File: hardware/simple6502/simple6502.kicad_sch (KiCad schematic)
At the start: 20 parts, among them J1 ~{VP}, J2 CLK SEL, J3 RESET, J7 FTDI Serial, J8 USB Power, SW1 RESET, T1 DS1813-10+, U1 W65C02SxP, U2 RAM 62256, U3 ROM 28C256, U4 74LS30, U5 74HCT00, U6 74HC138, U7 MC68B50, X1 ACO-1MHz

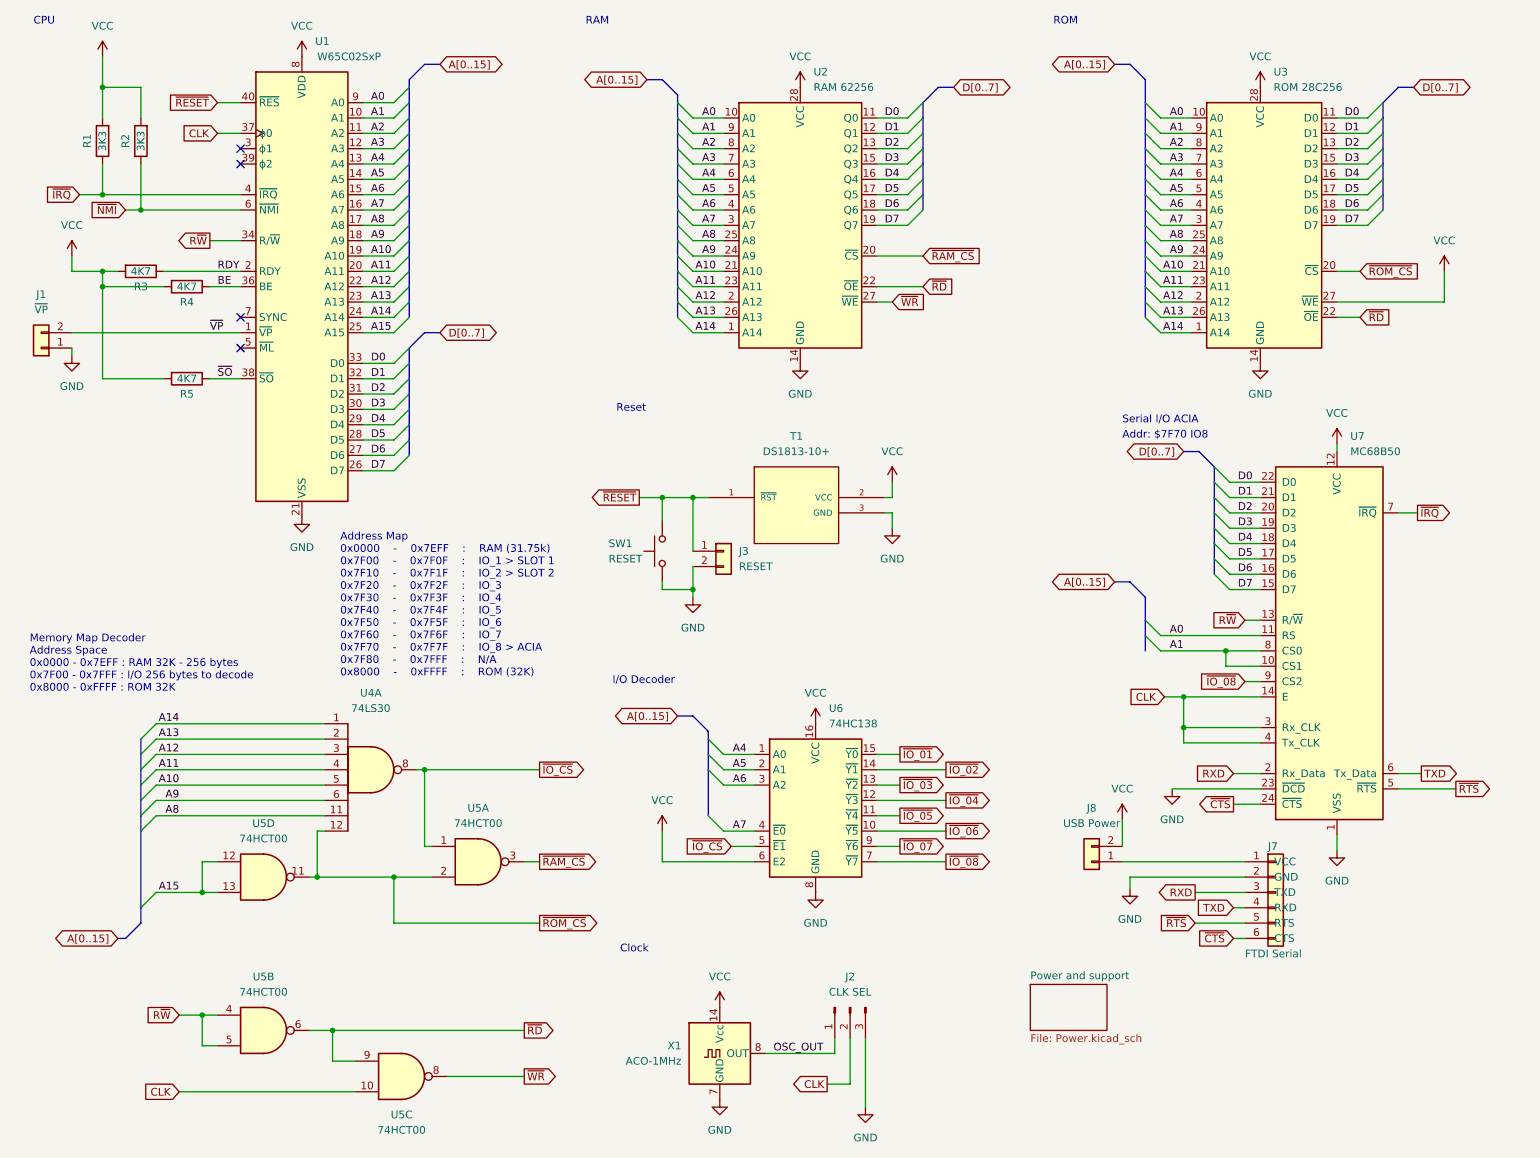
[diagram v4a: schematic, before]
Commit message: renumer components based on PCB placement
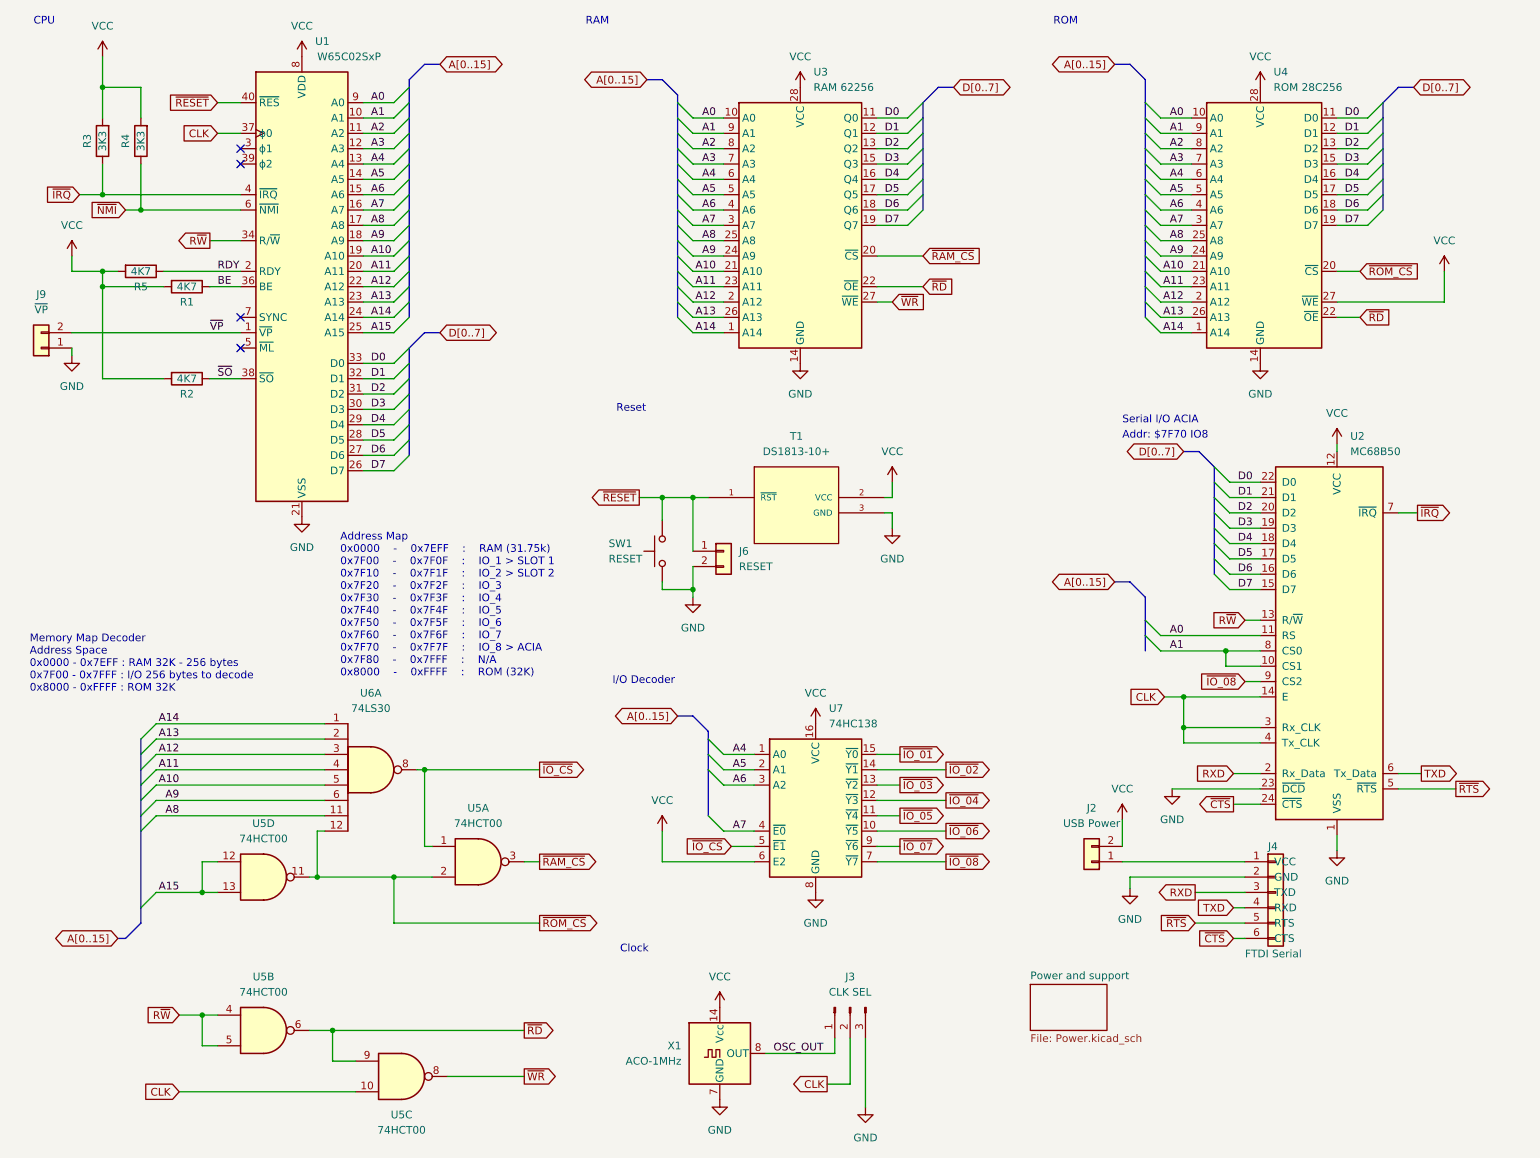
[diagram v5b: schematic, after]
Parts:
- renumbered J8 to J2, J2 to J3, J7 to J4, J3 to J6, J1 to J9, R4 to R1, R5 to R2, R1 to R3, R2 to R4, R3 to R5, U7 to U2, U2 to U3, U3 to U4, U4 to U6, U6 to U7
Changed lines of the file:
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@@
   (symbol (lib_id "Connector:Conn_01x03_Pin") (at 150.495 179.07 90) (mirror x) (unit 1)
     (in_bom yes) (on_board yes) (dnp no)
-    (property "Reference" "J2" (at 150.495 173.99 90)
+    (property "Reference" "J3" (at 150.495 173.99 90)
       (effects (font (size 1.27 1.27)))
     )
@@
       (project "simple6502"
         (path "/c0007eb4-077e-4f77-aad9-8dd15548af06"
-          (reference "J2") (unit 1)
+          (reference "J3") (unit 1)
         )
       )
@@
   (symbol (lib_name "R_1") (lib_id "Device:R") (at 40.64 59.69 270) (unit 1)
     (in_bom yes) (on_board yes) (dnp no)
-    (property "Reference" "R4" (at 40.64 62.23 90)
+    (property "Reference" "R1" (at 40.64 62.23 90)
       (effects (font (size 1.27 1.27)))
     )
@@
       (project "simple6502"
         (path "/c0007eb4-077e-4f77-aad9-8dd15548af06"
-          (reference "R4") (unit 1)
+          (reference "R1") (unit 1)
         )
       )
@@
   (symbol (lib_id "74xx:74LS30") (at 71.12 139.7 0) (unit 1)
     (in_bom yes) (on_board yes) (dnp no) (fields_autoplaced)
-    (property "Reference" "U4" (at 71.1117 127 0)
+    (property "Reference" "U6" (at 71.1117 127 0)
       (effects (font (size 1.27 1.27)))
     )
@@
       (project "simple6502"
         (path "/c0007eb4-077e-4f77-aad9-8dd15548af06"
-          (reference "U4") (unit 1)
+          (reference "U6") (unit 1)
         )
       )
@@
   (symbol (lib_name "R_1") (lib_id "Device:R") (at 26.67 35.56 180) (unit 1)
     (in_bom yes) (on_board yes) (dnp no)
-    (property "Reference" "R1" (at 24.13 35.56 90)
+    (property "Reference" "R3" (at 24.13 35.56 90)
       (effects (font (size 1.27 1.27)))
     )
@@
       (project "simple6502"
         (path "/c0007eb4-077e-4f77-aad9-8dd15548af06"
-          (reference "R1") (unit 1)
+          (reference "R3") (unit 1)
         )
       )
@@
   (symbol (lib_id "Memory_RAM:CY62256-70PC") (at 142.24 49.53 0) (unit 1)
     (in_bom yes) (on_board yes) (dnp no) (fields_autoplaced)
-    (property "Reference" "U2" (at 144.4341 24.13 0)
+    (property "Reference" "U3" (at 144.4341 24.13 0)
       (effects (font (size 1.27 1.27)) (justify left))
     )
@@
       (project "simple6502"
         (path "/c0007eb4-077e-4f77-aad9-8dd15548af06"
-          (reference "U2") (unit 1)
+          (reference "U3") (unit 1)
         )
       )
@@
   (symbol (lib_id "Memory_EEPROM:28C256") (at 218.44 54.61 0) (unit 1)
     (in_bom yes) (on_board yes) (dnp no) (fields_autoplaced)
-    (property "Reference" "U3" (at 220.6341 24.13 0)
+    (property "Reference" "U4" (at 220.6341 24.13 0)
       (effects (font (size 1.27 1.27)) (justify left))
     )
@@
       (project "simple6502"
         (path "/c0007eb4-077e-4f77-aad9-8dd15548af06"
-          (reference "U3") (unit 1)
+          (reference "U4") (unit 1)
         )
       )
@@
   (symbol (lib_id "74xx:74HC138") (at 144.78 147.32 0) (unit 1)
     (in_bom yes) (on_board yes) (dnp no) (fields_autoplaced)
-    (property "Reference" "U6" (at 146.9741 129.54 0)
+    (property "Reference" "U7" (at 146.9741 129.54 0)
       (effects (font (size 1.27 1.27)) (justify left))
     )
@@
       (project "simple6502"
         (path "/c0007eb4-077e-4f77-aad9-8dd15548af06"
-          (reference "U6") (unit 1)
+          (reference "U7") (unit 1)
         )
       )
@@
   (symbol (lib_id "Connector_Generic:Conn_01x06") (at 220.98 160.02 0) (unit 1)
     (in_bom yes) (on_board yes) (dnp no) (fields_autoplaced)
-    (property "Reference" "J7" (at 219.71 152.4 0)
+    (property "Reference" "J4" (at 219.71 152.4 0)
       (effects (font (size 1.27 1.27)) (justify left))
     )
@@
       (project "simple6502"
         (path "/c0007eb4-077e-4f77-aad9-8dd15548af06"
-          (reference "J7") (unit 1)
+          (reference "J4") (unit 1)
         )
       )
@@
   (symbol (lib_name "R_1") (lib_id "Device:R") (at 33.02 57.15 270) (unit 1)
     (in_bom yes) (on_board yes) (dnp no)
-    (property "Reference" "R3" (at 33.02 59.69 90)
+    (property "Reference" "R5" (at 33.02 59.69 90)
       (effects (font (size 1.27 1.27)))
     )
@@
       (project "simple6502"
         (path "/c0007eb4-077e-4f77-aad9-8dd15548af06"
-          (reference "R3") (unit 1)
+          (reference "R5") (unit 1)
         )
       )
@@
   (symbol (lib_id "Connector_Generic:Conn_01x02") (at 190.5 154.94 180) (unit 1)
     (in_bom yes) (on_board yes) (dnp no) (fields_autoplaced)
-    (property "Reference" "J8" (at 190.5 146.05 0)
+    (property "Reference" "J2" (at 190.5 146.05 0)
       (effects (font (size 1.27 1.27)))
     )
@@
       (project "simple6502"
         (path "/c0007eb4-077e-4f77-aad9-8dd15548af06"
-          (reference "J8") (unit 1)
+          (reference "J2") (unit 1)
         )
       )
@@
   (symbol (lib_id "Connector_Generic:Conn_01x02") (at 129.54 103.505 0) (unit 1)
     (in_bom yes) (on_board yes) (dnp no) (fields_autoplaced)
-    (property "Reference" "J3" (at 132.08 103.505 0)
+    (property "Reference" "J6" (at 132.08 103.505 0)
       (effects (font (size 1.27 1.27)) (justify left))
     )
@@
       (project "simple6502"
         (path "/c0007eb4-077e-4f77-aad9-8dd15548af06"
-          (reference "J3") (unit 1)
+          (reference "J6") (unit 1)
         )
       )
@@
   (symbol (lib_id "Interface_UART:MC68B50") (at 231.14 120.015 0) (unit 1)
     (in_bom yes) (on_board yes) (dnp no) (fields_autoplaced)
-    (property "Reference" "U7" (at 233.3341 84.455 0)
+    (property "Reference" "U2" (at 233.3341 84.455 0)
       (effects (font (size 1.27 1.27)) (justify left))
     )
@@
       (project "simple6502"
         (path "/c0007eb4-077e-4f77-aad9-8dd15548af06"
-          (reference "U7") (unit 1)
+          (reference "U2") (unit 1)
         )
       )
@@
   (symbol (lib_id "Connector_Generic:Conn_01x02") (at 16.51 69.85 180) (unit 1)
     (in_bom yes) (on_board yes) (dnp no) (fields_autoplaced)
-    (property "Reference" "J1" (at 16.51 60.96 0)
+    (property "Reference" "J9" (at 16.51 60.96 0)
       (effects (font (size 1.27 1.27)))
     )
@@
       (project "simple6502"
         (path "/c0007eb4-077e-4f77-aad9-8dd15548af06"
-          (reference "J1") (unit 1)
+          (reference "J9") (unit 1)
         )
       )
@@
   (symbol (lib_name "R_1") (lib_id "Device:R") (at 33.02 35.56 180) (unit 1)
     (in_bom yes) (on_board yes) (dnp no)
-    (property "Reference" "R2" (at 30.48 35.56 90)
+    (property "Reference" "R4" (at 30.48 35.56 90)
       (effects (font (size 1.27 1.27)))
     )
@@
       (project "simple6502"
         (path "/c0007eb4-077e-4f77-aad9-8dd15548af06"
-          (reference "R2") (unit 1)
+          (reference "R4") (unit 1)
         )
       )
@@
   (symbol (lib_name "R_1") (lib_id "Device:R") (at 40.64 74.93 270) (unit 1)
     (in_bom yes) (on_board yes) (dnp no)
-    (property "Reference" "R5" (at 40.64 77.47 90)
+    (property "Reference" "R2" (at 40.64 77.47 90)
       (effects (font (size 1.27 1.27)))
     )
@@
       (project "simple6502"
         (path "/c0007eb4-077e-4f77-aad9-8dd15548af06"
-          (reference "R5") (unit 1)
-        )
-      )
+          (reference "R2") (unit 1)
+        )
+      )

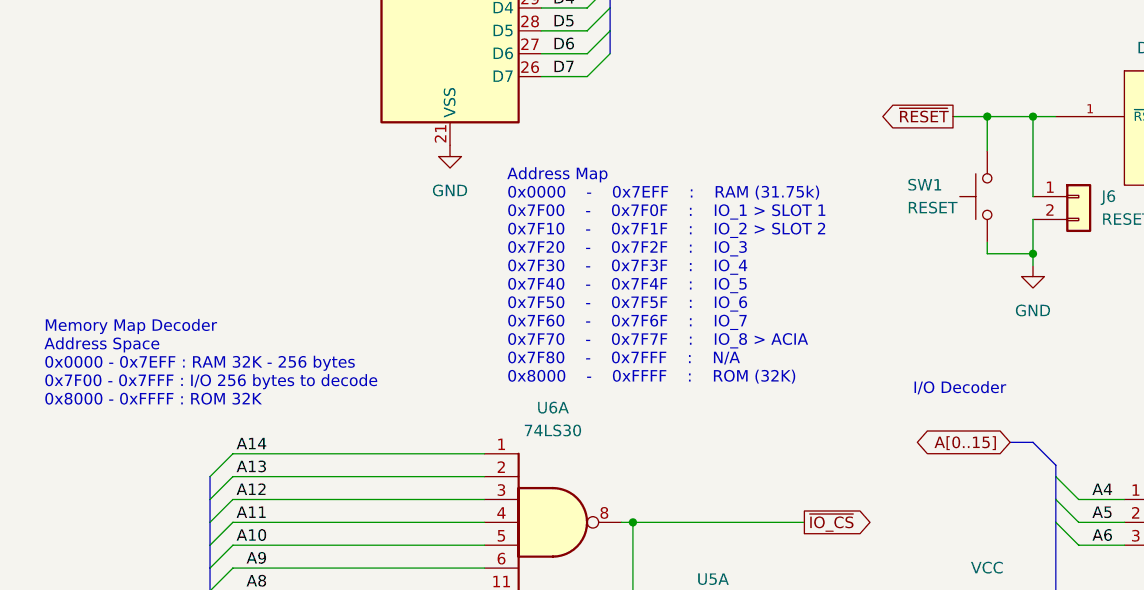
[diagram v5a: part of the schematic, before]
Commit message: updated ReadME and memory map in the schematic
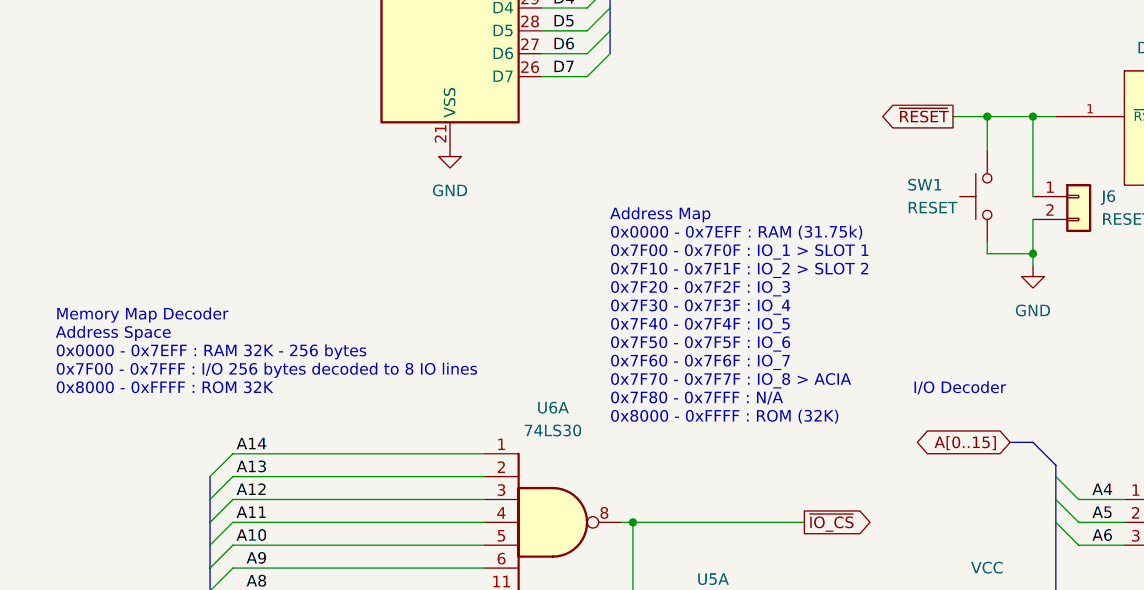
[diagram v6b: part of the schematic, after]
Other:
- note added: "Memory Map Decoder Address Space 0x0000 - 0x7EFF : RAM 32K - 256 bytes 0x7F00 - 0x7FFF : I/O 256 bytes decoded to 8 IO lines 0x8000 - 0xFFFF : ROM 32K"
- note removed: "Memory Map Decoder Address Space 0x0000 - 0x7EFF : RAM 32K - 256 bytes 0x7F00 - 0x7FFF : I/O 256 bytes to decode 0x8000 - 0xFFFF : ROM 32K"
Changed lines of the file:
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@@
     (effects (font (size 1.27 1.27)) (justify left bottom))
   )
-  (text "Memory Map Decoder\nAddress Space\n0x0000 - 0x7EFF : RAM 32K - 256 bytes\n0x7F00 - 0x7FFF : I/O 256 bytes to decode\n0x8000 - 0xFFFF : ROM 32K\n"
-    (at 14.605 127 0)
+  (text "Memory Map Decoder\nAddress Space\n0x0000 - 0x7EFF : RAM 32K - 256 bytes\n0x7F00 - 0x7FFF : I/O 256 bytes decoded to 8 IO lines\n0x8000 - 0xFFFF : ROM 32K\n"
+    (at 15.875 125.73 0)
     (effects (font (size 1.27 1.27)) (justify left bottom))
   )
@@
     (effects (font (size 1.27 1.27)) (justify left bottom))
   )
-  (text "Address Map				\n0x0000	-	0x7EFF	:	RAM (31.75k)\n0x7F00	-	0x7F0F	:	IO_1 > SLOT 1\n0x7F10	-	0x7F1F	:	IO_2 > SLOT 2\n0x7F20	-	0x7F2F	:	IO_3\n0x7F30	-	0x7F3F	:	IO_4\n0x7F40	-	0x7F4F	:	IO_5\n0x7F50	-	0x7F5F	:	IO_6\n0x7F60	-	0x7F6F	:	IO_7\n0x7F70	-	0x7F7F	:	IO_8 > ACIA\n0x7F80	-	0x7FFF	:	N/A\n0x8000	-	0xFFFF	:	ROM (32K)"
-    (at 66.04 124.46 0)
+  (text "Address Map				\n0x0000 - 0x7EFF : RAM (31.75k)\n0x7F00 - 0x7F0F : IO_1 > SLOT 1\n0x7F10 - 0x7F1F : IO_2 > SLOT 2\n0x7F20 - 0x7F2F : IO_3\n0x7F30 - 0x7F3F : IO_4\n0x7F40 - 0x7F4F : IO_5\n0x7F50 - 0x7F5F : IO_6\n0x7F60 - 0x7F6F : IO_7\n0x7F70 - 0x7F7F : IO_8 > ACIA\n0x7F80 - 0x7FFF : N/A\n0x8000 - 0xFFFF : ROM (32K)"
+    (at 77.47 128.905 0)
     (effects (font (size 1.27 1.27)) (justify left bottom))
   )
